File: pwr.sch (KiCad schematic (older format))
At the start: 64 parts, among them U1 FT601, U10 MIC94310, U11 PAM2305, U4 ECP5, U6 PAM2305, U7 NCP186, U8 MIC94310, U9 MIC94310, X2 CONN_01X08

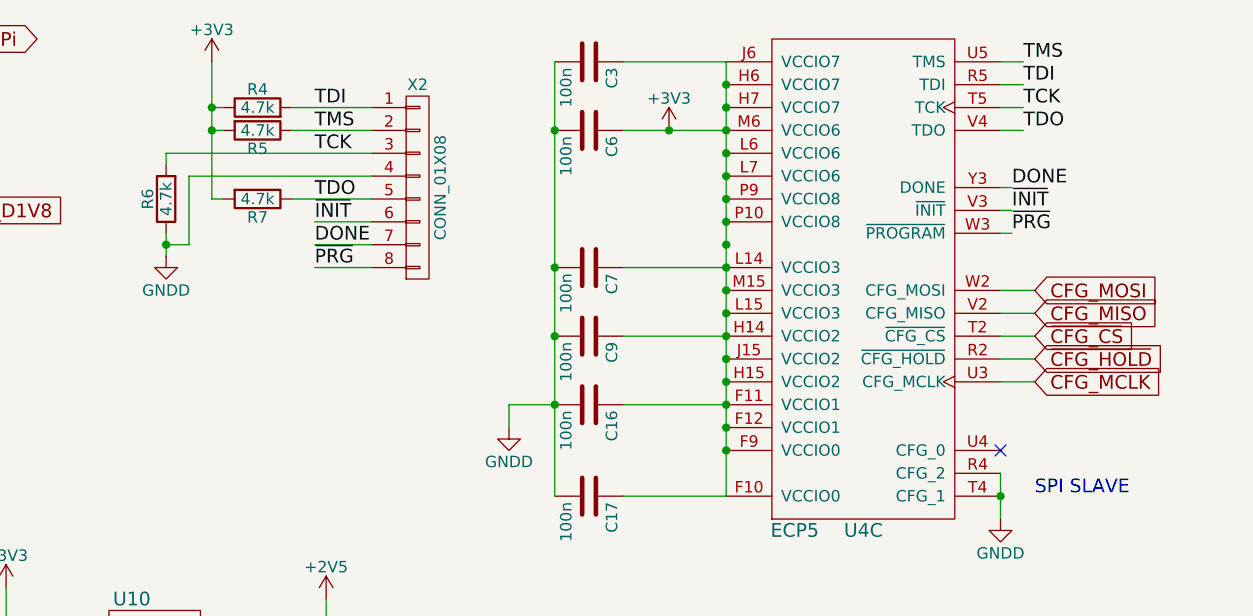
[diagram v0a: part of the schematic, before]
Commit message: FT232H has been finished Not finished: - PROGRAMN button - silkscreen preparation - RF
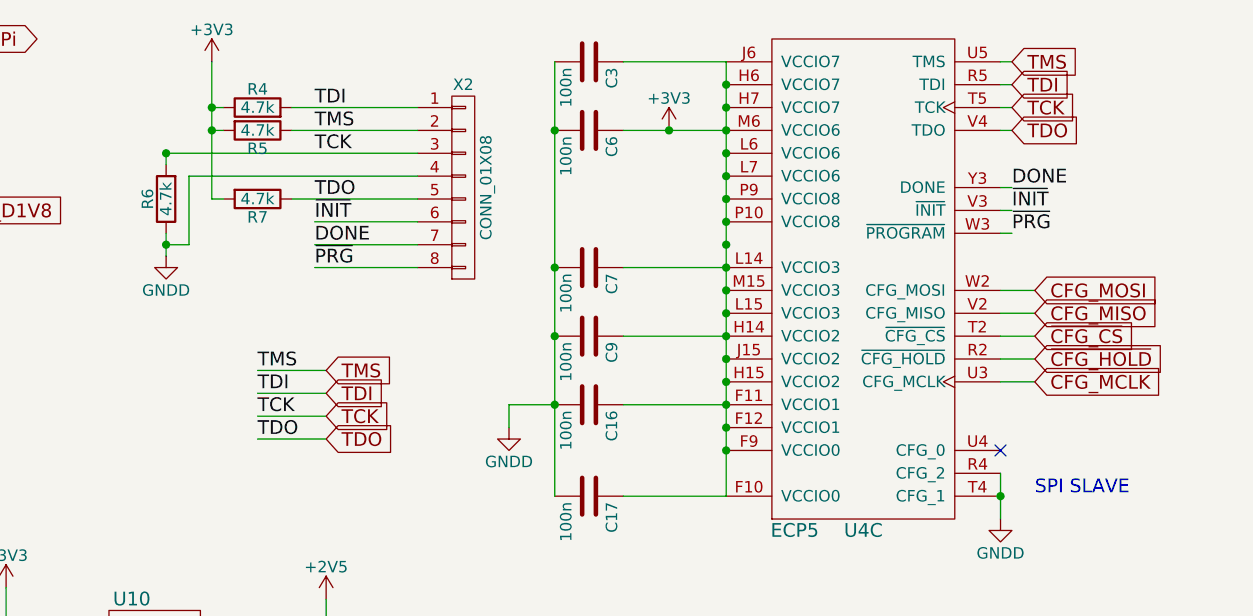
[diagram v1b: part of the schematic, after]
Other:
- moved on the sheet: X2

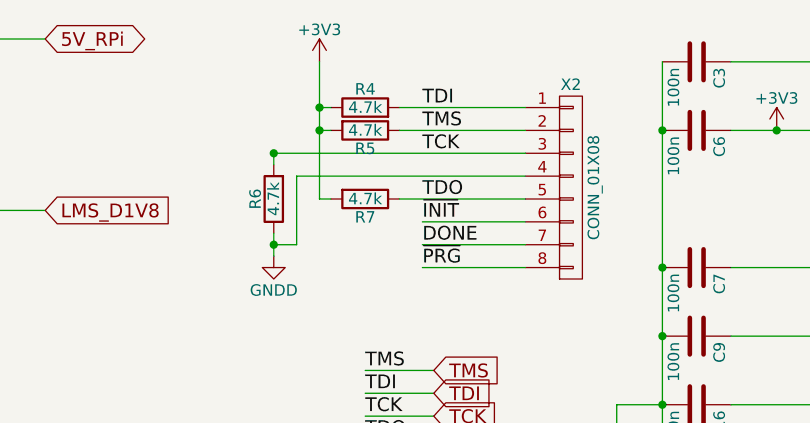
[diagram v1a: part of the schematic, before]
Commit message: Changed JTAG, added 0 Ohm resistors
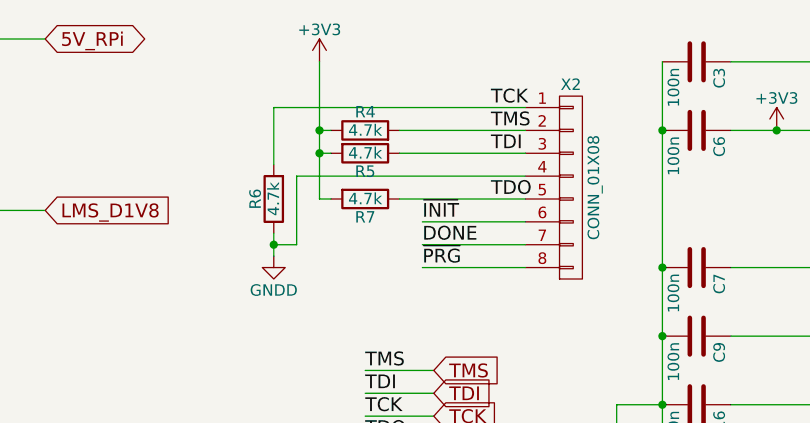
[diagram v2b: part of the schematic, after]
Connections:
- net TCK: now also X2.1 (P1); no longer X2.3 (P3)
- net TDI: now also R5.1, X2.3 (P3); no longer R4.2, X2.1 (P1)
- net TMS: now also R4.2; no longer R5.1
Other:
- moved on the sheet: R4, R5
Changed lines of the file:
@@
 L R R5
 U 1 1 589F2964
-P 6600 1250
-F 0 "R5" V 6680 1250 50  0000 C CNN
-F 1 "4.7k" V 6600 1250 50  0000 C CNN
-F 2 "Resistors_SMD:R_0603" V 6530 1250 50  0001 C CNN
-F 3 "" H 6600 1250 50  0000 C CNN
-	1    6600 1250
+P 6600 1350
+F 0 "R5" V 6680 1350 50  0000 C CNN
+F 1 "4.7k" V 6600 1350 50  0000 C CNN
+F 2 "Resistors_SMD:R_0603" V 6530 1350 50  0001 C CNN
+F 3 "" H 6600 1350 50  0000 C CNN
+	1    6600 1350
 	0    1    1    0
 $EndComp
-Text Label 6850 1250 0    60   ~ 0
+Text Label 7150 1250 0    60   ~ 0
 TMS
 Text Label 6850 1650 0    60   ~ 0
@@
 Text Label 6850 1850 0    60   ~ 0
 ~PRG
-Text Label 6850 1150 0    60   ~ 0
+Text Label 7150 1350 0    60   ~ 0
 TDI
-Text Label 6850 1550 0    60   ~ 0
+Text Label 7150 1550 0    60   ~ 0
 TDO
 $Comp
 L R R4
 U 1 1 589F04F1
-P 6600 1150
-F 0 "R4" V 6680 1150 50  0000 C CNN
-F 1 "4.7k" V 6600 1150 50  0000 C CNN
-F 2 "Resistors_SMD:R_0603" V 6530 1150 50  0001 C CNN
-F 3 "" H 6600 1150 50  0000 C CNN
-	1    6600 1150
+P 6600 1250
+F 0 "R4" V 6680 1250 50  0000 C CNN
+F 1 "4.7k" V 6600 1250 50  0000 C CNN
+F 2 "Resistors_SMD:R_0603" V 6530 1250 50  0001 C CNN
+F 3 "" H 6600 1250 50  0000 C CNN
+	1    6600 1250
 	0    -1   -1   0
 $EndComp
@@
 	6300 1450 7300 1450
 Wire Wire Line
-	6200 1400 6200 1350
-Wire Wire Line
-	6200 1350 7300 1350
-Connection ~ 6400 1150
-Wire Wire Line
-	6450 1150 6400 1150
+	6200 1150 6200 1400
 Connection ~ 6400 1250
 Wire Wire Line
@@
 	6750 1250 7300 1250
 Wire Wire Line
-	6750 1150 7300 1150
-Wire Wire Line
 	6850 1850 7300 1850
 Wire Wire Line
 	7300 1750 6850 1750
-Connection ~ 6200 1350
 Text Label 6600 2400 0    60   ~ 0
 TDI
@@
 Text Label 6600 2500 0    60   ~ 0
 TCK
-Text Label 6850 1350 0    60   ~ 0
+Text Label 7150 1150 0    60   ~ 0
 TCK
 Wire Wire Line
@@
 Wire Wire Line
 	6900 2600 6600 2600
+Wire Wire Line
+	7300 1350 6750 1350
+Wire Wire Line
+	6200 1150 7300 1150
+Wire Wire Line
+	6450 1350 6400 1350
+Connection ~ 6400 1350
 $EndSCHEMATC

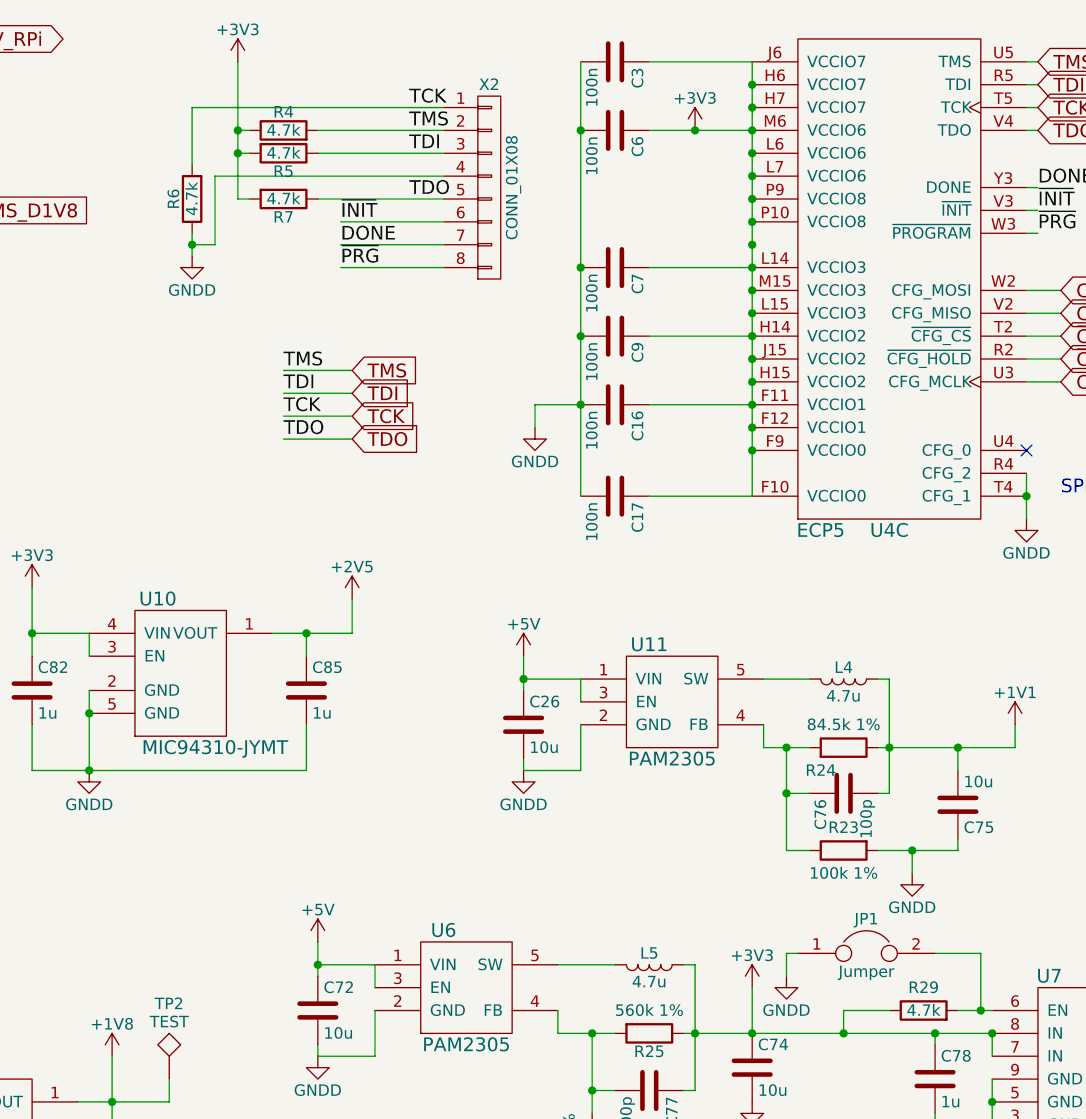
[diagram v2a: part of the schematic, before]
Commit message: Button is traced. Everything's ready to trace RF.
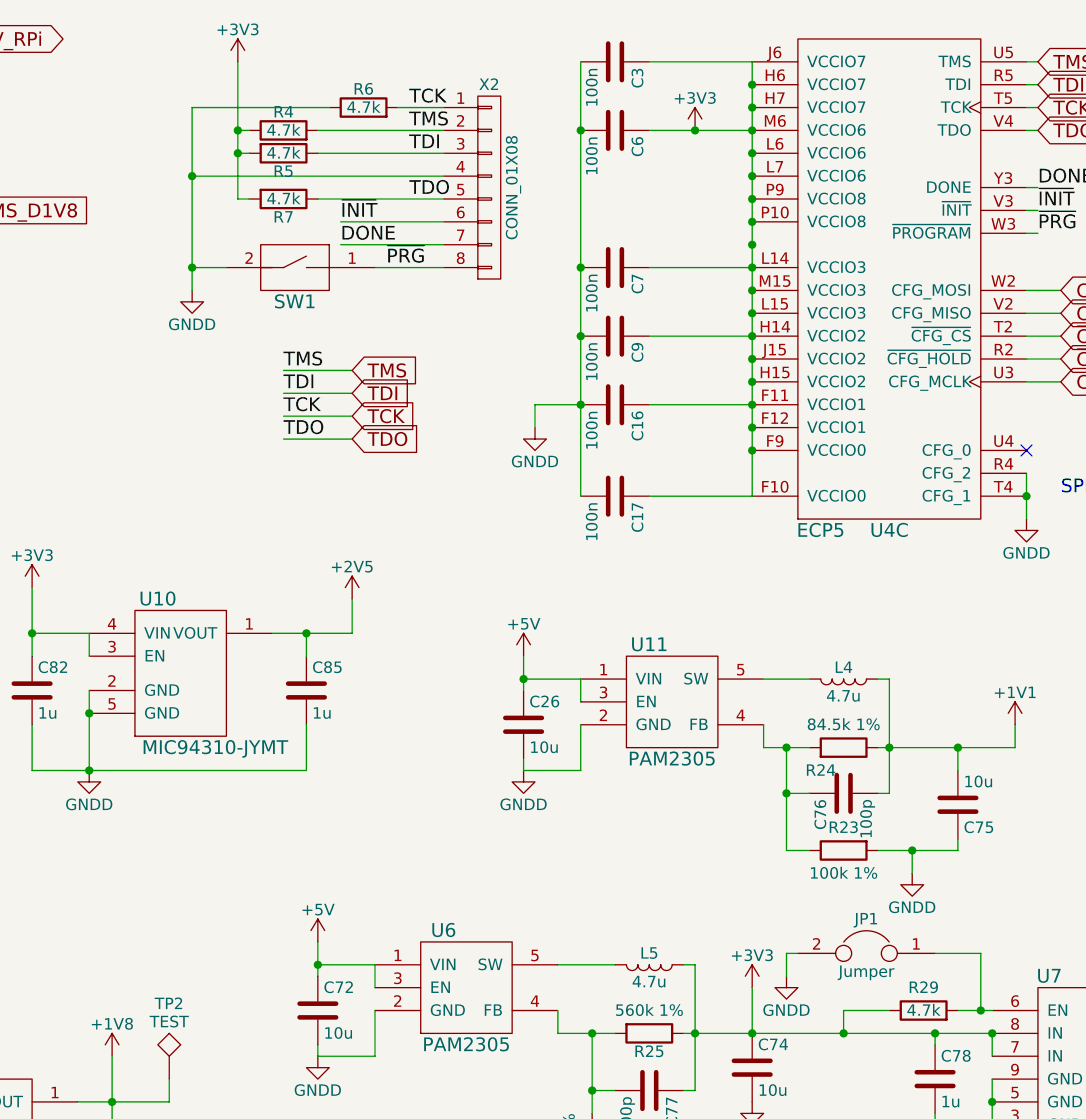
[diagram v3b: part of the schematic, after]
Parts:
- added SW1: Button, sdr-foots:Switch_KMR2, symbol Button
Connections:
- net GNDD: now also JP1.2, SW1.2; no longer JP1.1
- net ~PRG: now also SW1.1
- net at R29.2, U7.6 (EN): now also JP1.1; no longer JP1.2
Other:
- moved on the sheet: R6

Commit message: Added reference points. Right before RF tracing.
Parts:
- SW1: value Button -> KMR231NGLFS
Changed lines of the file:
@@
 P 6650 1950
 F 0 "SW1" H 6650 1900 60  0000 C CNN
-F 1 "Button" H 6650 1800 60  0001 C CNN
+F 1 "KMR231NGLFS" H 6650 1800 60  0001 C CNN
 F 2 "sdr-foots:Switch_KMR2" H 7300 1750 60  0001 C CNN
 F 3 "" H 7300 1750 60  0001 C CNN

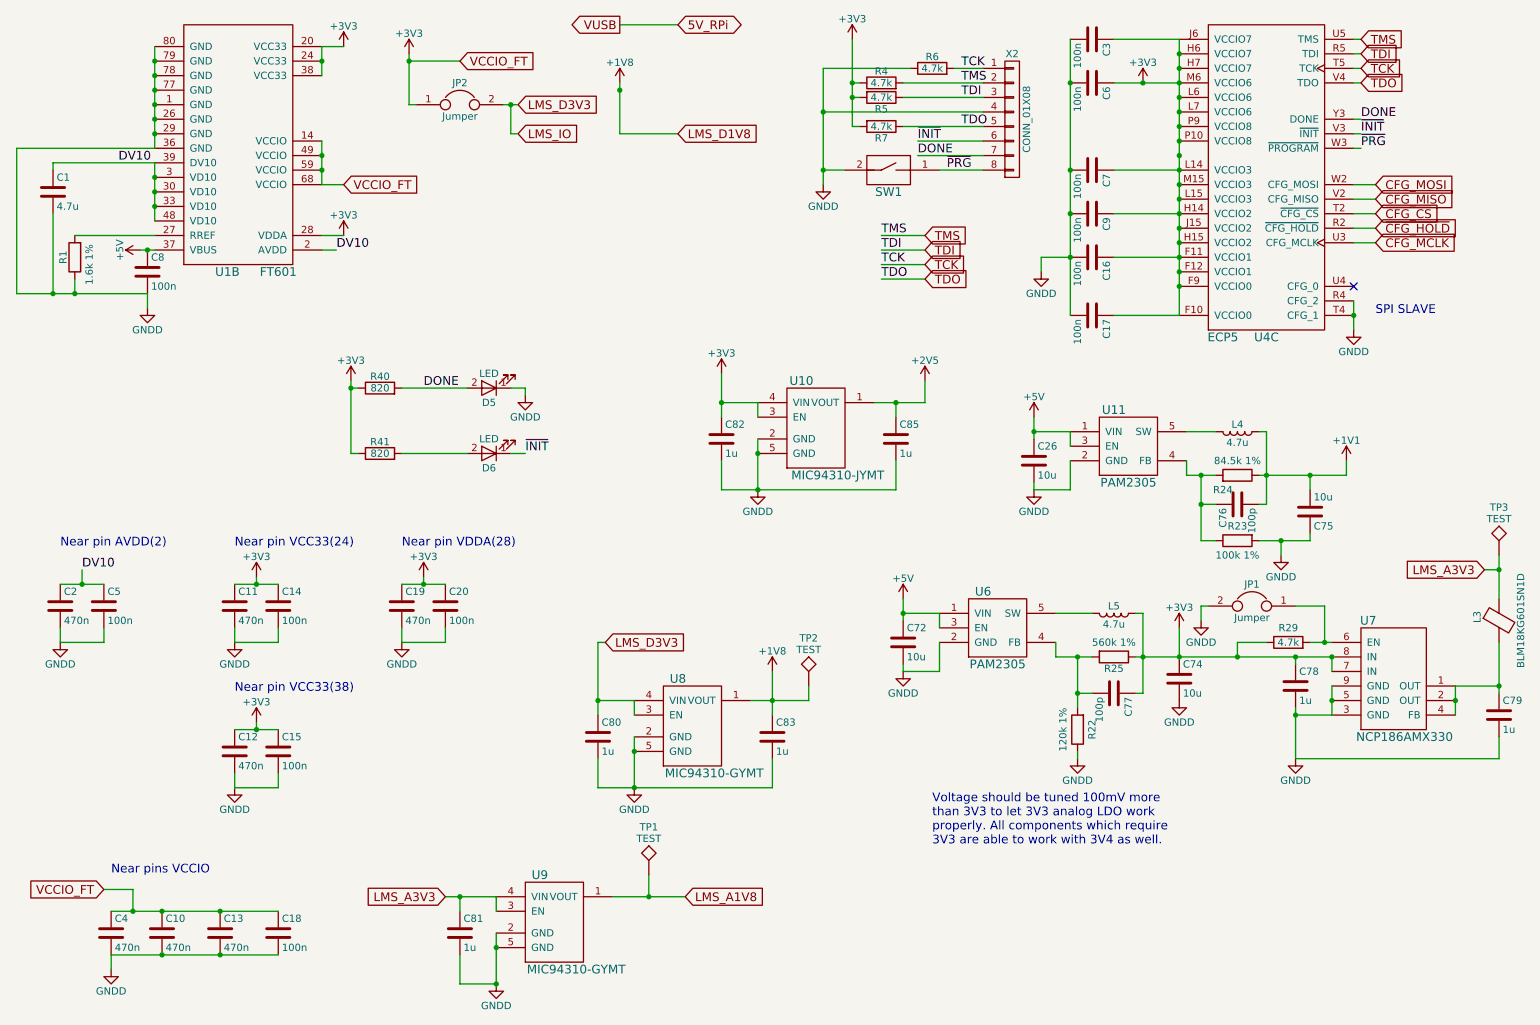
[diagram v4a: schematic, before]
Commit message: Finish silkscreen layer.
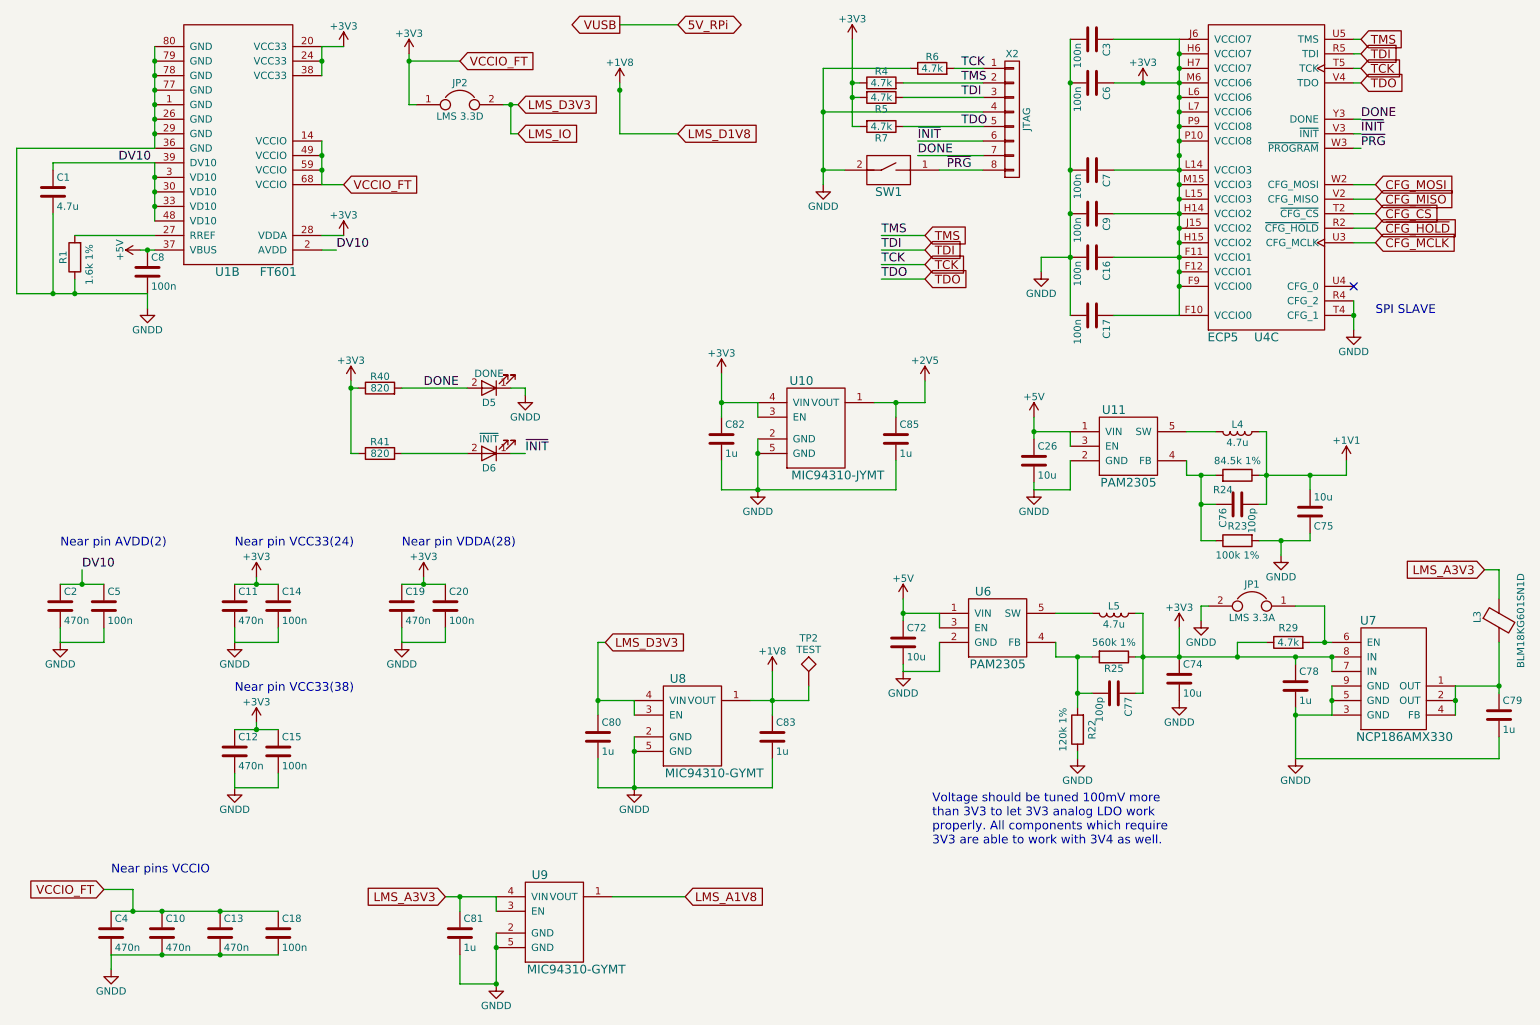
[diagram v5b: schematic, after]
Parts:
- removed TP1, TP3: TEST, Measurement_Points:Measurement_Point_Square-SMD-Pad_Small, symbol TEST
- D5: value LED -> DONE
- D6: value LED -> ~INIT
- JP1: value Jumper -> LMS 3.3A
- JP2: value Jumper -> LMS 3.3D
- SW1: Name (none) -> ~PROGRAM
- X2: value CONN_01X08 -> JTAG
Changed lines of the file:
@@
 P 9150 4850
 F 0 "JP1" H 9150 5000 50  0000 C CNN
-F 1 "Jumper" H 9150 4770 50  0000 C CNN
+F 1 "LMS 3.3A" H 9150 4770 50  0000 C CNN
 F 2 "Pin_Headers:Pin_Header_Angled_1x02_Pitch2.54mm" H 9150 4850 50  0001 C CNN
 F 3 "" H 9150 4850 50  0001 C CNN
@@
 P 3700 1400
 F 0 "JP2" H 3700 1550 50  0000 C CNN
-F 1 "Jumper" H 3700 1320 50  0000 C CNN
+F 1 "LMS 3.3D" H 3700 1320 50  0000 C CNN
 F 2 "Pin_Headers:Pin_Header_Angled_1x02_Pitch2.54mm" H 3700 1400 50  0001 C CNN
 F 3 "" H 3700 1400 50  0001 C CNN
 	1    3700 1400
-	1    0    0    -1
-$EndComp
-$Comp
-L TEST TP3
-U 1 1 59339CA4
-P 10850 4500
-F 0 "TP3" H 10850 4800 50  0000 C BNN
-F 1 "TEST" H 10850 4750 50  0000 C CNN
-F 2 "Measurement_Points:Measurement_Point_Square-SMD-Pad_Small" H 10850 4500 50  0001 C CNN
-F 3 "" H 10850 4500 50  0001 C CNN
-	1    10850 4500
-	1    0    0    -1
-$EndComp
-$Comp
-L TEST TP1
-U 1 1 5933A8A7
-P 5000 6700
-F 0 "TP1" H 5000 7000 50  0000 C BNN
-F 1 "TEST" H 5000 6950 50  0000 C CNN
-F 2 "Measurement_Points:Measurement_Point_Square-SMD-Pad_Small" H 5000 6700 50  0001 C CNN
-F 3 "" H 5000 6700 50  0001 C CNN
-	1    5000 6700
 	1    0    0    -1
 $EndComp
@@
 P 3900 3350
 F 0 "D5" H 3900 3450 50  0000 C CNN
-F 1 "LED" H 3900 3250 50  0000 C CNN
+F 1 "DONE" H 3900 3250 50  0000 C CNN
 F 2 "LEDs:LED_0603" H 3900 3350 50  0001 C CNN
 F 3 "" H 3900 3350 50  0001 C CNN
@@
 P 3900 3800
 F 0 "D6" H 3900 3900 50  0000 C CNN
-F 1 "LED" H 3900 3700 50  0000 C CNN
+F 1 "~INIT" H 3900 3700 50  0000 C CNN
 F 2 "LEDs:LED_0603" H 3900 3800 50  0001 C CNN
 F 3 "" H 3900 3800 50  0001 C CNN
@@
 P 7500 1500
 F 0 "X2" H 7500 1950 50  0000 C CNN
-F 1 "CONN_01X08" V 7600 1500 50  0000 C CNN
+F 1 "JTAG" V 7600 1500 50  0000 C CNN
 F 2 "Pin_Headers:Pin_Header_Straight_1x08_Pitch1.27mm" H 7500 1500 50  0001 C CNN
 F 3 "" H 7500 1500 50  0000 C CNN
@@
 F 2 "sdr-foots:Switch_KMR2" H 7300 1750 60  0001 C CNN
 F 3 "" H 7300 1750 60  0001 C CNN
+F 4 "~PROGRAM" H 6650 1950 60  0001 C CNN "Name"
 	1    6650 1950
 	-1   0    0    -1
@@
 	10850 5100 10850 5450
 Wire Wire Line
-	10850 4500 10850 4800
+	10850 4600 10850 4800
 Connection ~ 9450 5200
 Wire Wire Line
@@
 	4050 1600 4050 1400
 Connection ~ 4050 1400
-Connection ~ 10850 4600
-Wire Wire Line
-	5000 6700 5000 6850
-Connection ~ 5000 6850
 Wire Wire Line
 	6100 5500 6100 5400
